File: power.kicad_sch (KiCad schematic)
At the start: 13 parts, among them J4 Screw_Terminal_01x02, U1 4011, U10 LM2901, U11 4012, U16 L7805, U2 4011, U3 4011, U4 4011, U5 4011, U6 4011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

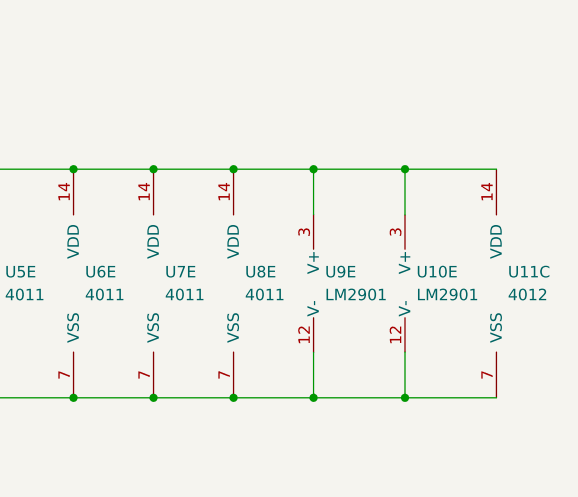
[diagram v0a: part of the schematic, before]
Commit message: Switch reset driver to MAX6895
Signed-off-by: Oliver Gaskell <og305@cam.ac.uk>
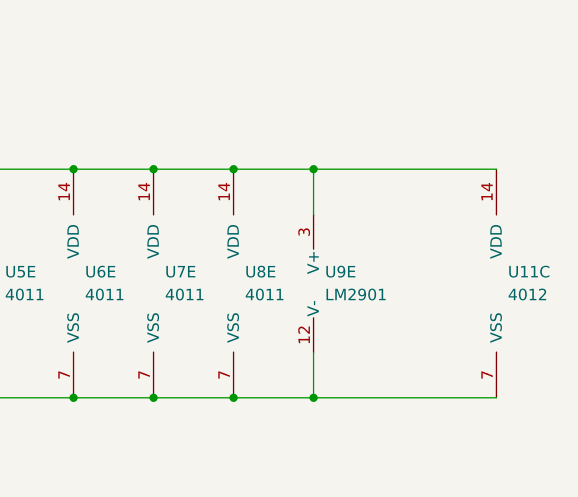
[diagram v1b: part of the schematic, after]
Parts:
- removed U10: LM2901, Package_DIP:DIP-14_W7.62mm_Socket, symbol Comparator:LM2901
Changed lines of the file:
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@@
-	)
-	(junction
-		(at 107.95 125.73)
-		(diameter 0)
-		(color 0 0 0 0)
 	)
 	(junction
@@
 	)
 	(junction
-		(at 107.95 100.33)
-		(diameter 0)
-		(color 0 0 0 0)
-	)
-	(junction
 		(at 97.79 125.73)
 		(diameter 0)
@@
 	(wire
 		(pts
-			(xy 118.11 125.73) (xy 107.95 125.73)
+			(xy 97.79 125.73) (xy 118.11 125.73)
 		)
 		(stroke
@@
 	(wire
 		(pts
-			(xy 107.95 125.73) (xy 97.79 125.73)
-		)
-		(stroke
-			(width 0)
-			(type default)
-		)
-	)
-	(wire
-		(pts
 			(xy 44.45 100.33) (xy 53.34 100.33)
 		)
@@
 	(wire
 		(pts
-			(xy 107.95 120.65) (xy 107.95 125.73)
-		)
-		(stroke
-			(width 0)
-			(type default)
-		)
-	)
-	(wire
-		(pts
 			(xy 71.12 125.73) (xy 80.01 125.73)
 		)
@@
 	(wire
 		(pts
-			(xy 107.95 100.33) (xy 118.11 100.33)
-		)
-		(stroke
-			(width 0)
-			(type default)
-		)
-	)
-	(wire
-		(pts
 			(xy 80.01 100.33) (xy 88.9 100.33)
 		)
@@
 	(wire
 		(pts
-			(xy 107.95 100.33) (xy 107.95 105.41)
-		)
-		(stroke
-			(width 0)
-			(type default)
-		)
-	)
-	(wire
-		(pts
 			(xy 68.58 33.02) (xy 66.04 33.02)
 		)
@@
 	(wire
 		(pts
-			(xy 97.79 100.33) (xy 107.95 100.33)
+			(xy 97.79 100.33) (xy 118.11 100.33)
 		)
 		(stroke
@@
 				)
 			)
-		)
-	)
-	(symbol
-		(lib_id "Comparator:LM2901")
-		(at 110.49 113.03 0)
-		(unit 5)
-		(exclude_from_sim no)
-		(in_bom yes)
-		(on_board yes)
-		(dnp no)
-		(fields_autoplaced yes)
-		(property "Reference" "U10"
-			(at 109.22 111.76 0)
-			(effects
-				(font
-					(size 1.27 1.27)
-				)
-				(justify left)
-			)
-		)
-		(property "Value" "LM2901"
-			(at 109.22 114.3 0)
-			(effects
-				(font
-					(size 1.27 1.27)
-				)
-				(justify left)
-			)
-		)
-		(property "Footprint" "Package_DIP:DIP-14_W7.62mm_Socket"
-			(at 109.22 110.49 0)
-			(effects
-				(font
-					(size 1.27 1.27)
-				)
-				(hide yes)
-			)
-		)
-		(property "Datasheet" "https://www.st.com/resource/en/datasheet/lm2901.pdf"
-			(at 111.76 107.95 0)
-			(effects
-				(font
-					(size 1.27 1.27)
-				)
-				(hide yes)
-			)
-		)
-		(property "Description" "Quad Differential Comparators, DIP-14/SOIC-14/TSSOP-14"
-			(at 110.49 113.03 0)
-			(effects
-				(font
-					(size 1.27 1.27)
-				)
-				(hide yes)
-			)
-		)
-		(pin "2"
-		)
-		(pin "4"
-		)
-		(pin "5"
-		)
-		(pin "1"
-		)
-		(pin "6"
-		)
-		(pin "7"
-		)
-		(pin "10"
-		)
-		(pin "11"
-		)
-		(pin "13"
-		)
-		(pin "14"
-		)
-		(pin "8"
-		)
-		(pin "9"
-		)
-		(pin "12"
-		)
-		(pin "3"
-		)
-		(instances
-			(project "New BSPD"
-				(path "/1f7c501a-057f-4634-92ce-528b01503799/6659f853-0940-49ae-bcda-2fedad30cd0c"
-					(reference "U10")
-					(unit 5)
-				)
-			)

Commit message: Complete new version
Signed-off-by: Oliver Gaskell <og305@cam.ac.uk>
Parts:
- removed J4: Screw_Terminal_01x02, BSPD_footprints:ATF13-2P-BM03, symbol Connector:Screw_Terminal_01x02
- removed U16: L7805, Package_TO_SOT_THT:TO-220-3_Horizontal_TabDown, symbol Regulator_Linear:L7805
- removed U8: 4011, Package_DIP:DIP-14_W7.62mm_Socket, symbol 4xxx:4011
- added C1: 0.1u, Capacitor_SMD:C_0603_1608Metric_Pad1.08x0.95mm_HandSolder, symbol Device:C_Small
- added C4: 1u, Capacitor_SMD:C_0603_1608Metric_Pad1.08x0.95mm_HandSolder, symbol Device:C_Polarized_Small_US
- added R14: 715, Resistor_SMD:R_0603_1608Metric_Pad0.98x0.95mm_HandSolder, symbol Device:R_Small
- added R8: 240, Resistor_SMD:R_0603_1608Metric_Pad0.98x0.95mm_HandSolder, symbol Device:R_Small
- added U10: LM317_SOT-223, Package_TO_SOT_SMD:SOT-223-3_TabPin2, symbol Regulator_Linear:LM317_SOT-223
- U9: value LM2901 -> TLC3704
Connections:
- net +12V: now also C1.1, U10.3 (VI)
- net +5V: now also C4.1, R8.1, U10.2 (VO)
- net GND: now also C1.2, C4.2, R14.2
- new net: R14.1, R8.2, U10.1 (ADJ)
